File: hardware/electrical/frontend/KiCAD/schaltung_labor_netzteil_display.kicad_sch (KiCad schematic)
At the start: 15 parts, among them J1 V_psu +, J10 SW+, J11 SW-, J2 V_psu -, J3 V_out +, J4 V_out -, J5 V_in +, J6 V_in -, J7 PWM, J8 U_in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

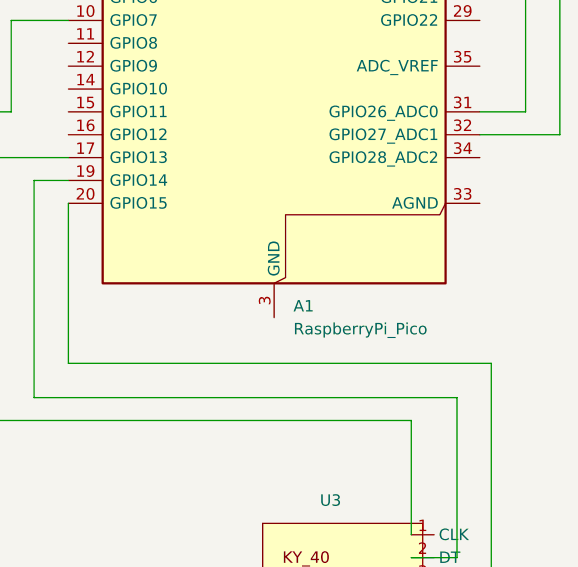
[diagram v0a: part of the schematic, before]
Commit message: Updated PCBs; added Bleed Resistor and fixed Frontend GND connections
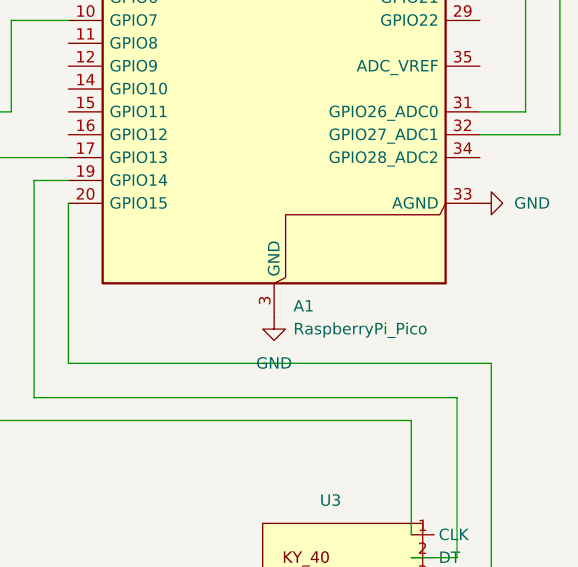
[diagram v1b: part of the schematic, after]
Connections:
- net GND: now also A1.13 (GND), A1.18 (GND), A1.23 (GND), A1.28 (GND), A1.3 (GND), A1.33 (AGND), A1.38 (GND), A1.8 (GND)
- net at U1.1 (CLK): now also A1.2 (GPIO1)
- net at U1.2 (DIO): now also A1.1 (GPIO0)
- net at U2.1 (CLK): now also A1.10 (GPIO7)
- net at U2.2 (DIO): now also A1.9 (GPIO6)
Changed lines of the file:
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@@
+	(symbol
+		(lib_id "power:GND")
+		(at 246.38 85.09 90)
+		(unit 1)
+		(exclude_from_sim no)
+		(in_bom yes)
+		(on_board yes)
+		(dnp no)
+		(fields_autoplaced yes)
+		(property "Reference" "#PWR06"
+			(at 252.73 85.09 0)
+			(effects
+				(font
+					(size 1.27 1.27)
+				)
+				(hide yes)
+			)
+		)
+		(property "Value" "GND"
+			(at 250.19 85.0899 90)
+			(effects
+				(font
+					(size 1.27 1.27)
+				)
+				(justify right)
+			)
+		)
+		(property "Footprint" ""
+			(at 246.38 85.09 0)
+			(effects
+				(font
+					(size 1.27 1.27)
+				)
+				(hide yes)
+			)
+		)
+		(property "Datasheet" ""
+			(at 246.38 85.09 0)
+			(effects
+				(font
+					(size 1.27 1.27)
+				)
+				(hide yes)
+			)
+		)
+		(property "Description" "Power symbol creates a global label with name \"GND\" , ground"
+			(at 246.38 85.09 0)
+			(effects
+				(font
+					(size 1.27 1.27)
+				)
+				(hide yes)
+			)
+		)
+		(pin "1"
+		)
+		(instances
+			(project ""
+				(path "/ed05b8dd-7d5c-45d2-9941-ff7e884565ed"
+					(reference "#PWR06")
+					(unit 1)
+				)
+			)
+		)
+	)
 	(symbol
 		(lib_id "power:GND")
@@
 					(unit 1)
 				)
+			)
+		)
+	)
+	(symbol
+		(lib_id "power:GND")
+		(at 223.52 97.79 0)
+		(unit 1)
+		(exclude_from_sim no)
+		(in_bom yes)
+		(on_board yes)
+		(dnp no)
+		(fields_autoplaced yes)
+		(property "Reference" "#PWR05"
+			(at 223.52 104.14 0)
+			(effects
+				(font
+					(size 1.27 1.27)
+				)
+				(hide yes)
+			)
+		)
+		(property "Value" "GND"
+			(at 223.52 102.87 0)
+			(effects
+				(font
+					(size 1.27 1.27)
+				)
+			)
+		)
+		(property "Footprint" ""
+			(at 223.52 97.79 0)
+			(effects
+				(font
+					(size 1.27 1.27)
+				)
+				(hide yes)
+			)
+		)
+		(property "Datasheet" ""
+			(at 223.52 97.79 0)
+			(effects
+				(font
+					(size 1.27 1.27)
+				)
+				(hide yes)
+			)
+		)
+		(property "Description" "Power symbol creates a global label with name \"GND\" , ground"
+			(at 223.52 97.79 0)
+			(effects
+				(font
+					(size 1.27 1.27)
+				)
+				(hide yes)
+			)
+		)
+		(pin "1"
+		)
+		(instances
+			(project ""
+				(path "/ed05b8dd-7d5c-45d2-9941-ff7e884565ed"
+					(reference "#PWR05")
+					(unit 1)
+				)
